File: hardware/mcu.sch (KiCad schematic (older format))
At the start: 23 parts, among them P3 CONN_2, P4 CONN_6, U13 USB-MICRO, U14 MKL26Z128VFT4, X1 8MHz

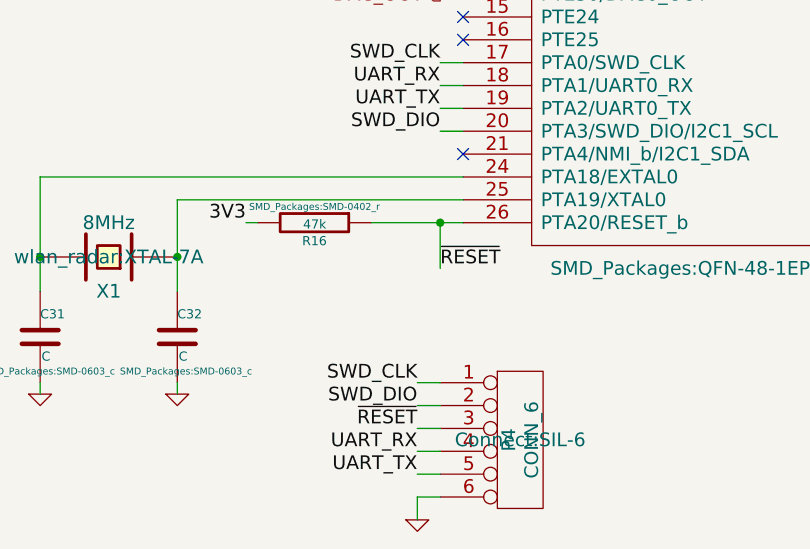
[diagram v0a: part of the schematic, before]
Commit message: Fix hardware mistakes
This commit adds fixes some of the mistakes identified after the
board was ordered.

Add 100n capacitor to MCUs reset pin to fix programming issues.

Add series connection of resistor and capacitor in parallel
with mixer output amplifier to fix the DC balance issue.

Remove the now unneeded capacitor and resistor
after the low-pass filter.

Add 200k resistor in feedback path of single-ended to differential
conversion circuit to solve the issue with limited input voltage range.
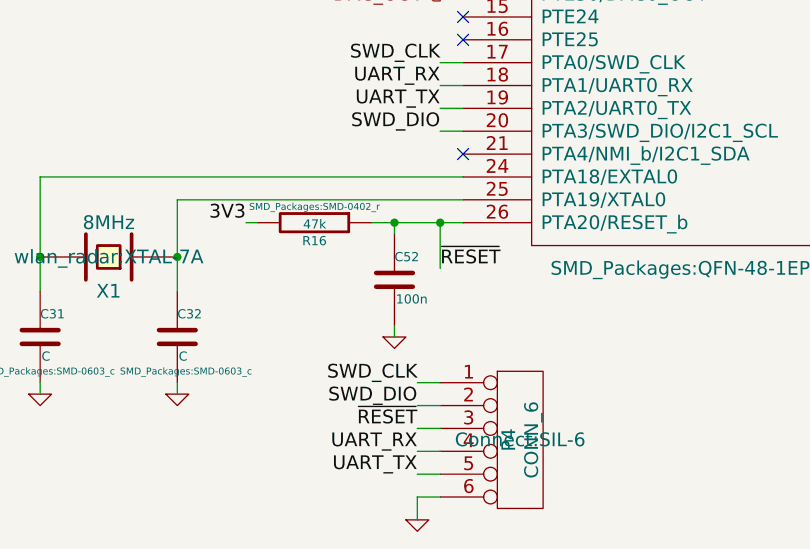
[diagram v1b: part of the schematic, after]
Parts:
- added C52: 100n, SMD_Packages:SMD-0402_c, symbol C
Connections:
- net GND: now also C52.2
- net ~RESET: now also C52.1
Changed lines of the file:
@@
 LIBS:valves
 LIBS:wlan_radar
-LIBS:sam_board
 LIBS:wlan_radar-cache
 EELAYER 25 0
@@
 Text HLabel 7800 2850 2    60   Output ~ 0
 PA_EN
+$Comp
+L C C52
+U 1 1 5480CAAD
+P 2250 5000
+F 0 "C52" H 2250 5100 40  0000 L CNN
+F 1 "100n" H 2256 4915 40  0000 L CNN
+F 2 "SMD_Packages:SMD-0402_c" H 2288 4850 30  0001 C CNN
+F 3 "" H 2250 5000 60  0000 C CNN
+	1    2250 5000
+	1    0    0    -1
+$EndComp
+Wire Wire Line
+	2250 4750 2250 4800
+Connection ~ 2250 4750
+Wire Wire Line
+	2250 5200 2250 5250
+$Comp
+L GND #PWR065
+U 1 1 5480CC49
+P 2250 5250
+F 0 "#PWR065" H 2250 5250 30  0001 C CNN
+F 1 "GND" H 2250 5180 30  0001 C CNN
+F 2 "" H 2250 5250 60  0000 C CNN
+F 3 "" H 2250 5250 60  0000 C CNN
+	1    2250 5250
+	1    0    0    -1
+$EndComp
 $EndSCHEMATC

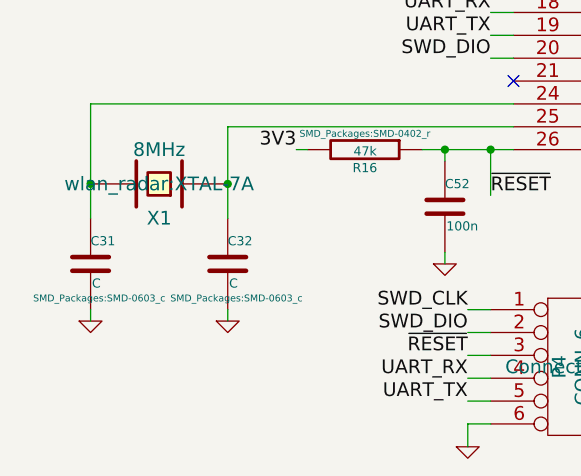
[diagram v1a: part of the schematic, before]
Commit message: Assign values to crystal load capacitors (33p)
Add 100n capacitors to BOM
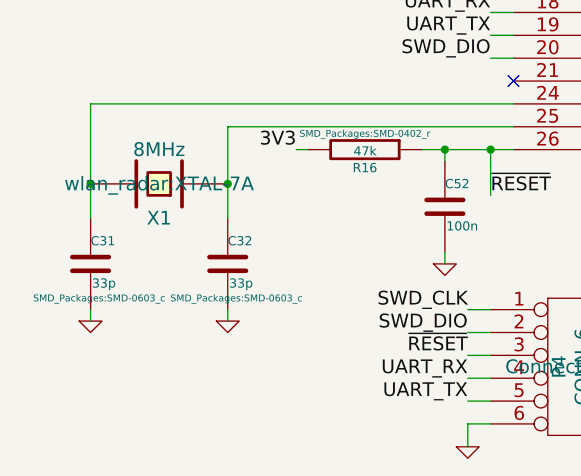
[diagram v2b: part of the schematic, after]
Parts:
- C31, C32: value C -> 33p
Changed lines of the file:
@@
 P 700 5250
 F 0 "C31" H 700 5350 40  0000 L CNN
-F 1 "C" H 706 5165 40  0000 L CNN
+F 1 "33p" H 706 5165 40  0000 L CNN
 F 2 "SMD_Packages:SMD-0603_c" H 738 5100 30  0000 C CNN
 F 3 "" H 700 5250 60  0000 C CNN
@@
 P 1300 5250
 F 0 "C32" H 1300 5350 40  0000 L CNN
-F 1 "C" H 1306 5165 40  0000 L CNN
+F 1 "33p" H 1306 5165 40  0000 L CNN
 F 2 "SMD_Packages:SMD-0603_c" H 1338 5100 30  0000 C CNN
 F 3 "" H 1300 5250 60  0000 C CNN
